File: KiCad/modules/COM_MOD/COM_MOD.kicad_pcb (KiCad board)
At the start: 4 copper layers, 15 x 15.8 mm, 14 parts, among them J1 Conn_01x01_Pin, J10 XF2J-1824-12A, J2 Conn_01x01_Pin, J3 Conn_01x01_Pin, J4 XF2J-1824-12A, J5 Conn_01x01_Pin, J6 Conn_01x01_Pin, J7 Conn_01x01_Pin, J8 Conn_01x01_Pin, J9 Conn_01x01_Pin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

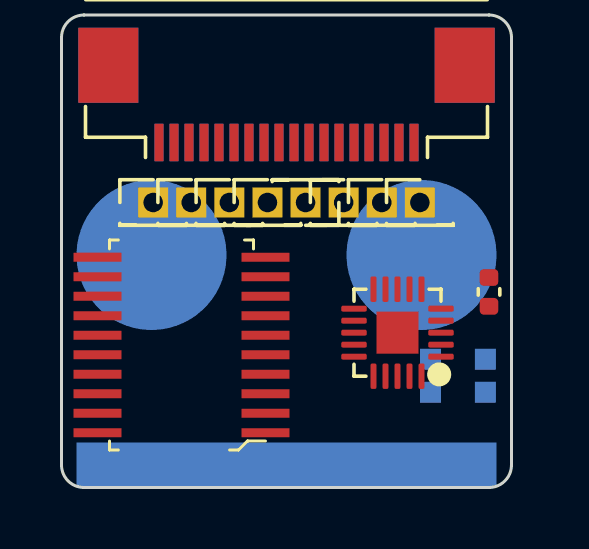
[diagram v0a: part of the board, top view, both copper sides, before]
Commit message: some cleaning + edge plating dry electrode
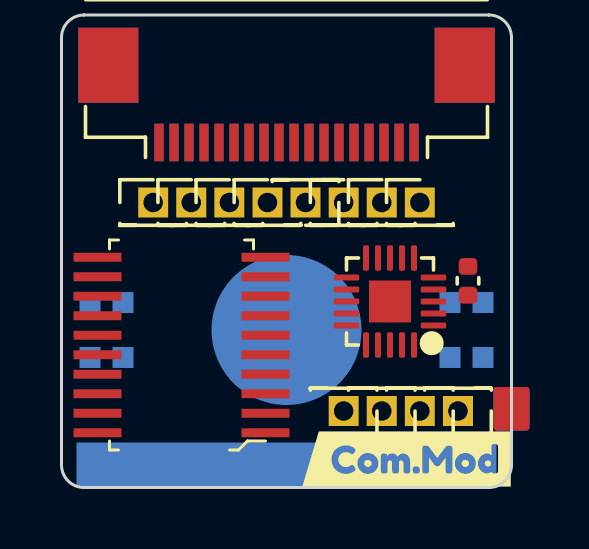
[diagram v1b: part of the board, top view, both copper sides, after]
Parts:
- added J11: Conn_01x01_Pin, Connector_PinHeader_1.27mm:PinHeader_1x01_P1.27mm_Vertical, F.Cu at (101.9, 110.7)
- added J12: Conn_01x01_Pin, Connector_PinHeader_1.27mm:PinHeader_1x01_P1.27mm_Vertical, F.Cu at (103.2, 110.7)
- added J13: Conn_01x01_Pin, Connector_PinHeader_1.27mm:PinHeader_1x01_P1.27mm_Vertical, F.Cu at (104.4, 110.7)
- added J14: Conn_01x01_Pin, Connector_PinHeader_1.27mm:PinHeader_1x01_P1.27mm_Vertical, F.Cu at (105.7, 110.7)
- added LED2: WS2812-2020, 00_custom-footprints:WS2812-2020, B.Cu at (94.0, 108.0)
- added kibuzzard-6569F493: G***, kibuzzard-6569F493, F.Cu at (104.0, 112.3)
- moved LED1 1.55 mm to (106.0, 108.0), turned to -90 degrees
- moved U1 1.07 mm to (103.5, 107.0)
- moved C1 0.79 mm to (106.0, 106.4), turned to 90 degrees
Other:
- board text added: "Aightech"
- board text added: "By"

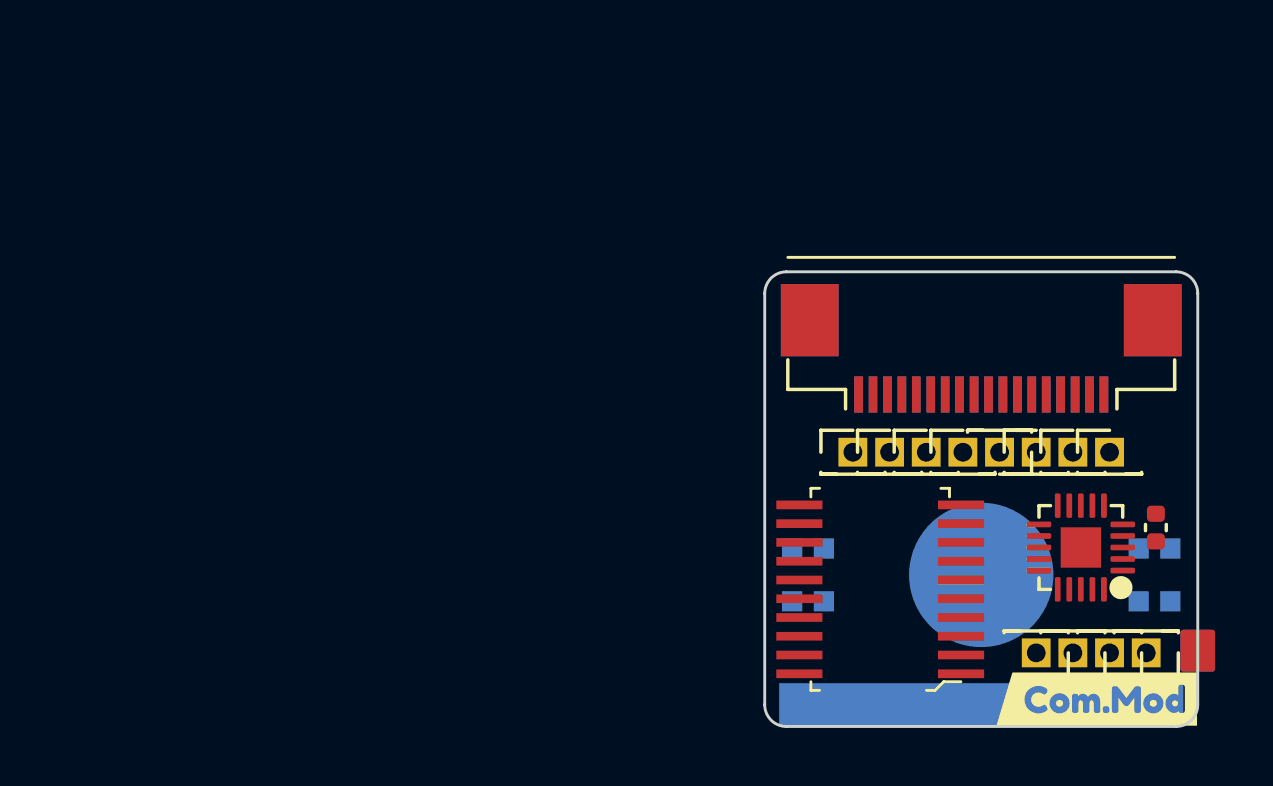
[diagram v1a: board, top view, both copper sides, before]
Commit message: finished rooting emgdaq + schematic commod
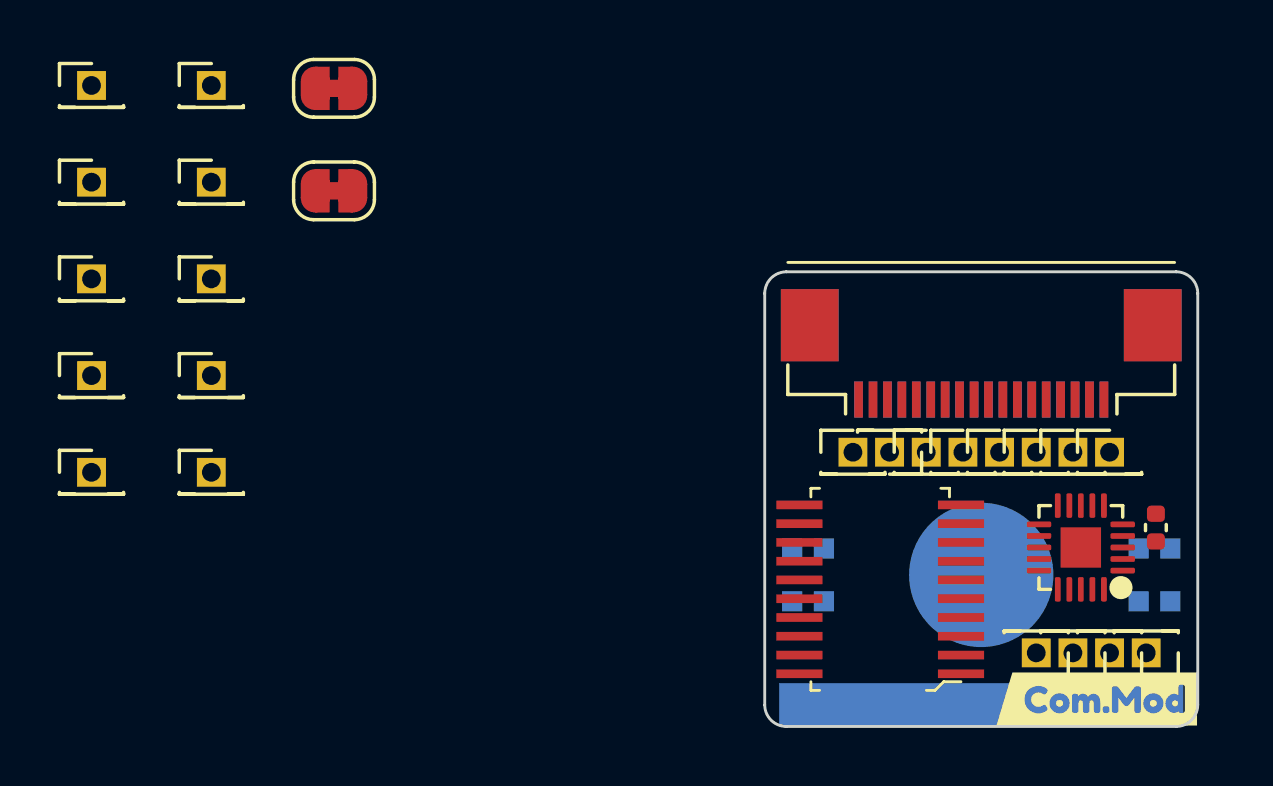
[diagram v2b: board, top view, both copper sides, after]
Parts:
- added J15: Conn_01x01_Pin, Connector_PinHeader_1.27mm:PinHeader_1x01_P1.27mm_Vertical, F.Cu at (69.2, 91.0)
- added J16: Conn_01x01_Pin, Connector_PinHeader_1.27mm:PinHeader_1x01_P1.27mm_Vertical, F.Cu at (69.2, 94.4)
- added J17: Conn_01x01_Pin, Connector_PinHeader_1.27mm:PinHeader_1x01_P1.27mm_Vertical, F.Cu at (69.2, 97.7)
- added J18: Conn_01x01_Pin, Connector_PinHeader_1.27mm:PinHeader_1x01_P1.27mm_Vertical, F.Cu at (69.2, 101.1)
- added J19: Conn_01x01_Pin, Connector_PinHeader_1.27mm:PinHeader_1x01_P1.27mm_Vertical, F.Cu at (69.2, 104.4)
- added J20: Conn_01x01_Pin, Connector_PinHeader_1.27mm:PinHeader_1x01_P1.27mm_Vertical, F.Cu at (73.3, 91.0)
- added J21: Conn_01x01_Pin, Connector_PinHeader_1.27mm:PinHeader_1x01_P1.27mm_Vertical, F.Cu at (73.3, 94.4)
- added J22: Conn_01x01_Pin, Connector_PinHeader_1.27mm:PinHeader_1x01_P1.27mm_Vertical, F.Cu at (73.3, 97.7)
- added J23: Conn_01x01_Pin, Connector_PinHeader_1.27mm:PinHeader_1x01_P1.27mm_Vertical, F.Cu at (73.3, 101.1)
- added J24: Conn_01x01_Pin, Connector_PinHeader_1.27mm:PinHeader_1x01_P1.27mm_Vertical, F.Cu at (73.3, 104.4)
- added JP1: SolderJumper_2_Bridged, Jumper:SolderJumper-2_P1.3mm_Bridged_RoundedPad1.0x1.5mm, F.Cu at (77.6, 91.1)
- added JP2: SolderJumper_2_Bridged, Jumper:SolderJumper-2_P1.3mm_Bridged_RoundedPad1.0x1.5mm, F.Cu at (77.6, 94.7)
- J10, J4: footprint Connector_FFC-FPC:XUNPU_FPC_05F_18P_H20 -> 00_custom-footprints:XUNPU_FPC_05F_18P_H20
- moved J1 8.89 mm to (95.6, 103.8)
- moved J9 5.08 mm to (104.4, 103.8)
- moved J2 3.81 mm to (96.8, 103.8)
- moved J7 3.81 mm to (101.9, 103.8)
- moved J3 2.54 mm to (98.1, 103.8)
- moved J5 2.54 mm to (99.4, 103.8)
- moved J6 1.27 mm to (100.6, 103.8)
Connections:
- J1 pad 1: unconnected-(J1-Pin_1-Pad1) -> +3.3V
- J10 pad 1: unconnected-(J10-Pad1) -> /extRef
- J10 pad 10: unconnected-(J10-Pad10) -> /addr_bus_3
- J10 pad 11: unconnected-(J10-Pad11) -> /addr_bus_2
- J10 pad 12: unconnected-(J10-Pad12) -> /addr_bus_1
- J10 pad 13: unconnected-(J10-Pad13) -> /addr_bus_0
- J10 pad 14: unconnected-(J10-Pad14) -> /SCLK
- J10 pad 15: unconnected-(J10-Pad15) -> /MOSI
- J10 pad 16: unconnected-(J10-Pad16) -> /MISO
- J10 pad 17: unconnected-(J10-Pad17) -> GND
- J10 pad 18: unconnected-(J10-Pad18) -> +3.3V
- J10 pad 2: unconnected-(J10-Pad2) -> /AUX3
- J10 pad 3: unconnected-(J10-Pad3) -> /AUX2
- J10 pad 4: unconnected-(J10-Pad4) -> /AUX1
- J10 pad 5: unconnected-(J10-Pad5) -> /BUS_IO2
- J10 pad 6: unconnected-(J10-Pad6) -> /BUS_IO1
- J10 pad 7: unconnected-(J10-Pad7) -> /I2C_SDA
- J10 pad 8: unconnected-(J10-Pad8) -> /i2C_SCL
- J10 pad 9: unconnected-(J10-Pad9) -> /addr_bus_4
- J11 pad 1: unconnected-(J11-Pin_1-Pad1) -> /SWCLK
- J12 pad 1: unconnected-(J12-Pin_1-Pad1) -> /SWDIO/MISO_ARM
- J13 pad 1: unconnected-(J13-Pin_1-Pad1) -> /MOSI_ARM
- J14 pad 1: unconnected-(J14-Pin_1-Pad1) -> /SCLK_ARM
- J2 pad 1: unconnected-(J2-Pin_1-Pad1) -> GND
- J4 pad 1: unconnected-(J4-Pad1) -> +3.3V
- J4 pad 10: unconnected-(J4-Pad10) -> /addr_bus_4
- J4 pad 11: unconnected-(J4-Pad11) -> /i2C_SCL
- J4 pad 12: unconnected-(J4-Pad12) -> /I2C_SDA
- J4 pad 13: unconnected-(J4-Pad13) -> /BUS_IO1
- J4 pad 14: unconnected-(J4-Pad14) -> /BUS_IO2
- J4 pad 15: unconnected-(J4-Pad15) -> /AUX1
- J4 pad 16: unconnected-(J4-Pad16) -> /AUX2
- J4 pad 17: unconnected-(J4-Pad17) -> /AUX3
- J4 pad 18: unconnected-(J4-Pad18) -> /extRef
- J4 pad 2: unconnected-(J4-Pad2) -> GND
- J4 pad 3: unconnected-(J4-Pad3) -> /MISO
- J4 pad 4: unconnected-(J4-Pad4) -> /MOSI
- J4 pad 5: unconnected-(J4-Pad5) -> /SCLK
- J4 pad 6: unconnected-(J4-Pad6) -> /addr_bus_0
- J4 pad 7: unconnected-(J4-Pad7) -> /addr_bus_1
- J4 pad 8: unconnected-(J4-Pad8) -> /addr_bus_2
- J4 pad 9: unconnected-(J4-Pad9) -> /addr_bus_3
- J5 pad 1: unconnected-(J5-Pin_1-Pad1) -> /MISO
- J6 pad 1: unconnected-(J6-Pin_1-Pad1) -> /MOSI
- J7 pad 1: unconnected-(J7-Pin_1-Pad1) -> /SCLK
- J8 pad 1: unconnected-(J8-Pin_1-Pad1) -> /CSB
- J9 pad 1: unconnected-(J9-Pin_1-Pad1) -> /extRef
- LED1 pad 1: LED_OUT -> Net-(LED1-DO)
- LED2 pad 3: LED_IN -> Net-(LED1-DO)
- U1 pad 11: unconnected-(U1-P24-Pad11) -> /AIN0
- U1 pad 12: unconnected-(U1-P25-Pad12) -> /SCLK_ARM
- U1 pad 13: unconnected-(U1-P26-Pad13) -> /MOSI_ARM
- U1 pad 14: unconnected-(U1-P27-Pad14) -> /SWDIO/MISO_ARM
- U1 pad 15: unconnected-(U1-P31-Pad15) -> /SWCLK
- U1 pad 16: unconnected-(U1-P32-Pad16) -> /addr_mod_2
- U1 pad 17: unconnected-(U1-P33-Pad17) -> /addr_mod_1
- U1 pad 18: unconnected-(U1-P34-Pad18) -> /addr_mod_0
- U1 pad 19: unconnected-(U1-P35-Pad19) -> /I2C_SDA
- U1 pad 2: unconnected-(U1-P01-Pad2) -> /NEOPIXEL
- U1 pad 20: unconnected-(U1-P36-Pad20) -> /i2C_SCL
- U1 pad 3: unconnected-(U1-P02-Pad3) -> /AIN8
- U1 pad 7: unconnected-(U1-P03-Pad7) -> /addr_mod_3
- U1 pad 8: unconnected-(U1-P15-Pad8) -> /addr_mod_4
- U1 pad 9: unconnected-(U1-P14-Pad9) -> /SPICS_ARM
- U2 pad 1: unconnected-(U2-G-Pad1) -> GND
- U2 pad 10: unconnected-(U2-GND-Pad10) -> GND
- U2 pad 11: unconnected-(U2-P4-Pad11) -> /addr_mod_4
- U2 pad 12: unconnected-(U2-R4-Pad12) -> /addr_bus_4
- U2 pad 13: unconnected-(U2-P5-Pad13) -> /addr_mod_5
- U2 pad 14: unconnected-(U2-R5-Pad14) -> /addr_bus_5
- U2 pad 15: unconnected-(U2-P6-Pad15) -> /addr_mod_6
- U2 pad 16: unconnected-(U2-R6-Pad16) -> /addr_bus_6
- U2 pad 17: unconnected-(U2-P7-Pad17) -> /addr_mod_7
- U2 pad 18: unconnected-(U2-R7-Pad18) -> /addr_bus_7
- U2 pad 19: unconnected-(U2-P=R-Pad19) -> /CSB
- U2 pad 2: unconnected-(U2-P0-Pad2) -> /addr_mod_0
- U2 pad 20: unconnected-(U2-VCC-Pad20) -> +3.3V
- U2 pad 3: unconnected-(U2-R0-Pad3) -> /addr_bus_0
- U2 pad 4: unconnected-(U2-P1-Pad4) -> /addr_mod_1
- U2 pad 5: unconnected-(U2-R1-Pad5) -> /addr_bus_1
- U2 pad 6: unconnected-(U2-P2-Pad6) -> /addr_mod_2
- U2 pad 7: unconnected-(U2-R2-Pad7) -> /addr_bus_2
- U2 pad 8: unconnected-(U2-P3-Pad8) -> /addr_mod_3
- U2 pad 9: unconnected-(U2-R3-Pad9) -> /addr_bus_3

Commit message: lot of updates on ads93,flex,commod,pad
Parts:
- removed J22, J23, J24: Conn_01x01_Pin, Connector_PinHeader_1.27mm:PinHeader_1x01_P1.27mm_Vertical
- removed JP1, JP2: SolderJumper_2_Bridged, Jumper:SolderJumper-2_P1.3mm_Bridged_RoundedPad1.0x1.5mm
- removed kibuzzard-6569F493: G***, kibuzzard-6569F493
- added I1: smd_insert, 00_Custom:insert_1.2mm, B.Cu at (30.0, 33.5)
- added R1: 10K, Resistor_SMD:R_0402_1005Metric, B.Cu at (24.1, 35.0)
- added SW1: NA, 00_Custom:SW-SMD_L3.9-W3.0-P4.45, B.Cu at (26.2, 37.4)
- added kibuzzard-658C2757: G***, kibuzzard-658C2757, B.Cu at (30.0, 31.8)
- added kibuzzard-658C3FF8: G***, kibuzzard-658C3FF8, F.Cu at (30.0, 39.1)
- J10: footprint 00_custom-footprints:XUNPU_FPC_05F_18P_H20 -> 00_Custom:XUNPU_FPC_05F_18P_H20; moved to F.Cu
- J4: footprint 00_custom-footprints:XUNPU_FPC_05F_18P_H20 -> 00_Custom:XUNPU_FPC_05F_18P_H20; moved to B.Cu
- LED1, LED2: footprint 00_custom-footprints:WS2812-2020 -> 00_Custom:WS2812-2020
- U1: footprint 00_custom-footprints:QFN-20-1EP_3x3mm_P0.4mm_EP1.4x1.4mm -> 00_Custom:QFN-20-1EP_3x3mm_P0.4mm_EP1.4x1.4mm
- moved C1 104.6 mm to (33.4, 31.2), turned to 180 degrees
- moved J3 104.3 mm to (30.0, 24.8)
- moved J14 104.1 mm to (32.8, 36.5)
- moved LED1 102.6 mm to (36.0, 33.0)
- moved LED2 102.6 mm to (24.0, 33.0), turned to 90 degrees
- moved J13 102.3 mm to (34.0, 36.5)
- moved J1 101.7 mm to (25.6, 30.0)
- moved J10 101.7 mm to (30.0, 28.0), turned to 180 degrees
- moved J2 101.7 mm to (26.8, 30.0)
- moved J4 101.7 mm to (30.0, 28.0), turned to 0 degrees
- moved J5 101.7 mm to (29.4, 30.0)
- moved J6 101.7 mm to (30.6, 30.0)
- moved J7 101.7 mm to (31.9, 30.0)
- moved J8 101.7 mm to (33.2, 30.0)
- moved J9 101.7 mm to (34.4, 30.0)
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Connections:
- net /BUS_IO2 renamed /IO2
- net LED_OUT renamed /LED_OUT
- J10 pad 10: /addr_bus_3 -> /addr_bus_4
- J10 pad 11: /addr_bus_2 -> /addr_bus_3
- J10 pad 12: /addr_bus_1 -> /addr_bus_2
- J10 pad 13: /addr_bus_0 -> /addr_bus_1
- J10 pad 14: /SCLK -> /addr_bus_0
- J10 pad 15: /MOSI -> /AUX3
- J10 pad 16: /MISO -> GND
- J10 pad 17: GND -> +3.3V
- J10 pad 18: +3.3V -> /AUX1
- J10 pad 2: /AUX3 -> /AUX2
- J10 pad 3: /AUX2 -> /i2C_SCL
- J10 pad 4: /AUX1 -> /I2C_SDA
- J10 pad 6: /BUS_IO1 -> /IO1_out
- J10 pad 7: /I2C_SDA -> /SCLK
- J10 pad 8: /i2C_SCL -> /MOSI
- J10 pad 9: /addr_bus_4 -> /MISO
- J11 pad 1: /SWCLK -> /IO1_out
- J18 pad 1: /AIN8 -> /AIN0
- J19 pad 1: /AIN0 -> /AUX1
- J20 pad 1: +3.3V -> /AUX2
- J21 pad 1: GND -> /GPIO
- J3 pad 1: unconnected-(J3-Pin_1-Pad1) -> /AUX3
- J4 pad 1: +3.3V -> /AUX1
- J4 pad 10: /addr_bus_4 -> /MISO
- J4 pad 11: /i2C_SCL -> /MOSI
- J4 pad 12: /I2C_SDA -> /SCLK
- J4 pad 13: /BUS_IO1 -> /IO1_in
- J4 pad 15: /AUX1 -> /I2C_SDA
- J4 pad 16: /AUX2 -> /i2C_SCL
- J4 pad 17: /AUX3 -> /AUX2
- J4 pad 2: GND -> +3.3V
- J4 pad 3: /MISO -> GND
- J4 pad 4: /MOSI -> /AUX3
- J4 pad 5: /SCLK -> /addr_bus_0
- J4 pad 6: /addr_bus_0 -> /addr_bus_1
- J4 pad 7: /addr_bus_1 -> /addr_bus_2
- J4 pad 8: /addr_bus_2 -> /addr_bus_3
- J4 pad 9: /addr_bus_3 -> /addr_bus_4
- LED1 pad 3: LED_IN -> /LED_IN
- U1 pad 10: unconnected-(U1-P23-Pad10) -> /GPIO
- U1 pad 15: /SWCLK -> /IO1_out
- U1 pad 2: /NEOPIXEL -> /LED_IN
- U1 pad 3: /AIN8 -> /IO1_in
- U2 pad 13: /addr_mod_5 -> GND
- U2 pad 14: /addr_bus_5 -> GND
- U2 pad 15: /addr_mod_6 -> GND
- U2 pad 16: /addr_bus_6 -> GND
- U2 pad 17: /addr_mod_7 -> GND
- U2 pad 18: /addr_bus_7 -> GND
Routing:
- net GND: track 0.00 -> 30.8 mm, vias 0 -> 24
- net +3.3V: track 0.00 -> 26.7 mm, vias 0 -> 1
- net /IO1_out: track 0.00 -> 19.7 mm, vias 0 -> 2
- net /i2C_SCL: track 0.00 -> 19.6 mm, vias 0 -> 2
- net /I2C_SDA: track 0.00 -> 18.4 mm, vias 0 -> 1
- net /addr_mod_0: track 0.00 -> 17.2 mm, vias 0 -> 2
- net /GPIO: track 0.00 -> 16.9 mm
- net /addr_bus_3: track 0.00 -> 15.9 mm, vias 0 -> 1
- net /addr_mod_1: track 0.00 -> 15.0 mm, vias 0 -> 2
- net /addr_mod_2: track 0.00 -> 14.8 mm, vias 0 -> 2
- net Net-(LED1-DO): track 0.00 -> 14.6 mm
- net /addr_bus_4: track 0.00 -> 13.5 mm, vias 0 -> 1
- net /addr_bus_2: track 0.00 -> 13.4 mm, vias 0 -> 1
- net /addr_bus_1: track 0.00 -> 12.5 mm, vias 0 -> 1
- net /IO1_in: track 0.00 -> 12.2 mm, vias 0 -> 1
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- added copper zone on B.Cu, net GND
- added copper zone on F.Cu, net GND
- added copper zone on In1.Cu, net GND
- added copper zone on In2.Cu, net GND
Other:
- board size 15 x 15.8 mm -> 15 x 16.3 mm
- board text added: "(SPI, I2C)"
- board text added: "PCB3D_BR_COM_MOD"
- board text added: "PCB3D_TL_COM_MOD"
- board text removed: "Aightech"
- board text removed: "By"

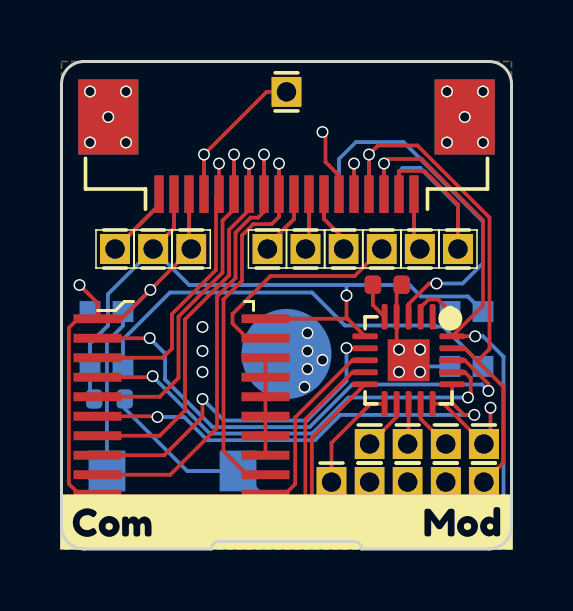
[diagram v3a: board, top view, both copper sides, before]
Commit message: finished ads93,commod,drypad,flexpad,jackconn,imubno + plot and render
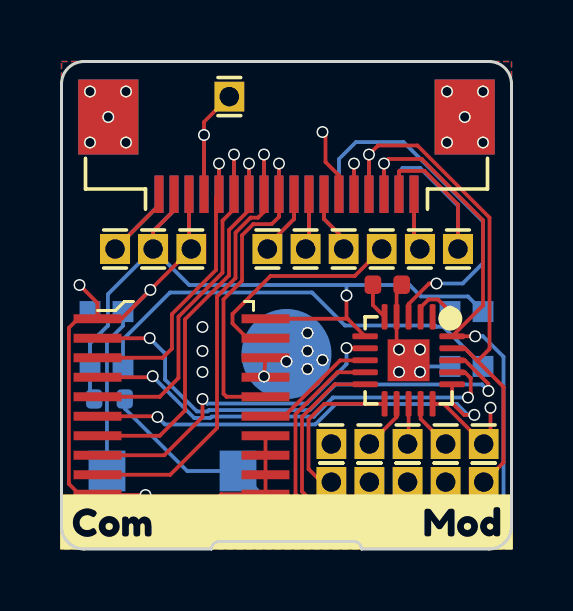
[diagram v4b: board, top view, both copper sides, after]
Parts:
- added J23: Conn_01x01_Pin, Connector_PinHeader_1.27mm:PinHeader_1x01_P1.27mm_Vertical, F.Cu at (31.5, 36.5)
- moved J3 1.91 mm to (28.1, 24.9)
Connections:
- U2 pad 11: /addr_mod_4 -> GND
- U2 pad 12: /addr_bus_4 -> GND
- U2 pad 15: GND -> /addr_mod_4
- U2 pad 16: GND -> /addr_bus_4
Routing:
- net GND: track 30.8 -> 34.7 mm, vias 24 -> 27
- net /addr_mod_4: track 6.47 -> 4.09 mm
- net /addr_bus_4: track 13.5 -> 11.3 mm
- net /AIN0: track 3.62 -> 5.35 mm
- net /GPIO: track 16.9 -> 17.7 mm
- net /addr_mod_3: track 12.0 -> 11.2 mm
- net /AUX3: track 6.26 -> 5.58 mm
- net /SPICS_ARM: track 9.29 -> 9.86 mm

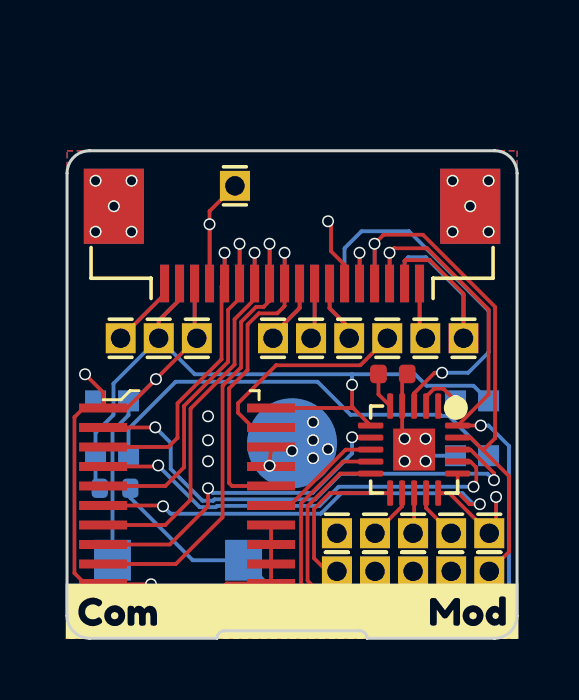
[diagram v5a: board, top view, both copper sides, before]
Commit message: refactor and fixing most of the modules
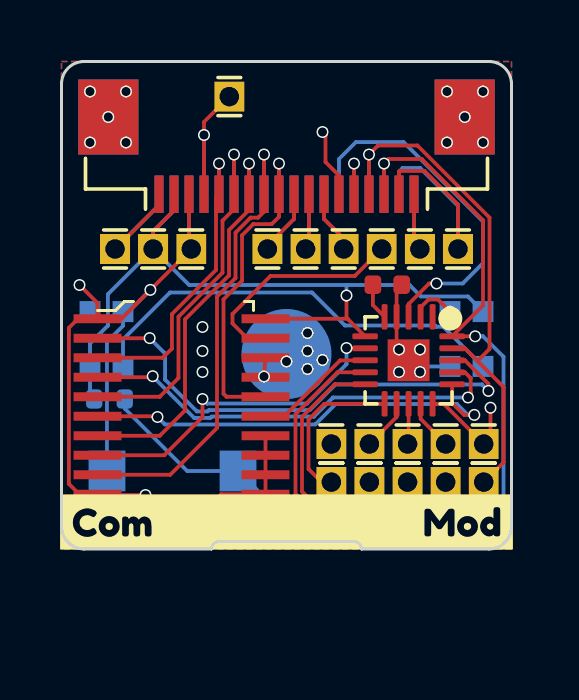
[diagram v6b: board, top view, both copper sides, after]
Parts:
- moved C1 2.98 mm to (33.2, 28.2)
- moved J1 2.98 mm to (25.4, 27.0)
- moved J10 2.98 mm to (29.8, 25.0)
- moved J11 2.98 mm to (36.4, 33.5)
- moved J12 2.98 mm to (35.1, 33.5)
- moved J13 2.98 mm to (33.9, 33.5)
- moved J14 2.98 mm to (32.6, 33.5)
- moved J16 2.98 mm to (35.1, 34.8)
- moved J17 2.98 mm to (36.4, 34.8)
- moved J18 2.98 mm to (31.3, 34.8)
- moved J19 2.98 mm to (24.1, 27.0)
- moved J20 2.98 mm to (35.5, 27.0)
- moved J21 2.98 mm to (32.6, 34.8)
- moved J23 2.98 mm to (31.3, 33.5)
- moved J4 2.98 mm to (29.8, 25.0)
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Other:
- outline, holes or cut-outs redrawn

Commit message: cleaned all modules + production files
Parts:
- FPC1: renamed from J4; value XF2J-1824-12A -> FPC-05F-18PH20; footprint 00_Custom:XUNPU_FPC_05F_18P_H20 -> 00_lcsc:FPC-SMD_18P-P0.50_FPC-05F-18PH20
- FPC2: renamed from J10; value XF2J-1824-12A -> FPC-05F-18PH20; footprint 00_Custom:XUNPU_FPC_05F_18P_H20 -> 00_lcsc:FPC-SMD_18P-P0.50_FPC-05F-18PH20
- moved FPC1 1.15 mm to (29.8, 23.9)
- moved FPC2 1.15 mm to (29.8, 23.9)
- renumbered J23 to J22

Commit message: updated
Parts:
- LED1: value WS2812-2020 -> WS2812C-2020-V1; footprint 00_Custom:WS2812-2020 -> 00_lcsc:LED-SMD_4P-L2.0-W2.0-TL_WS2812B-2020
- LED2: value WS2812-2020 -> WS2812C; footprint 00_Custom:WS2812-2020 -> 00_lcsc:LED-SMD_4P-L2.0-W2.0-TL_WS2812B-2020
- SW1: value NA -> TS-1088R-02026; footprint 00_Custom:SW-SMD_L3.9-W3.0-P4.45 -> 00_lcsc:SW-SMD_L3.9-W3.0-P4.45
- turned LED1 to 90 degrees
- turned LED2 to -90 degrees
